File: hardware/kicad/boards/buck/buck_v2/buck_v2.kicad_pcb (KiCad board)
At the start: 2 copper layers, 104 x 104 mm, 23 parts, among them J1 MCP PWM, J2 9V Battery, J3 Conn_01x02_Socket, Q1 IRF530, SW1 Switch, U1 LM7805, U2 4N25, U3 NE555

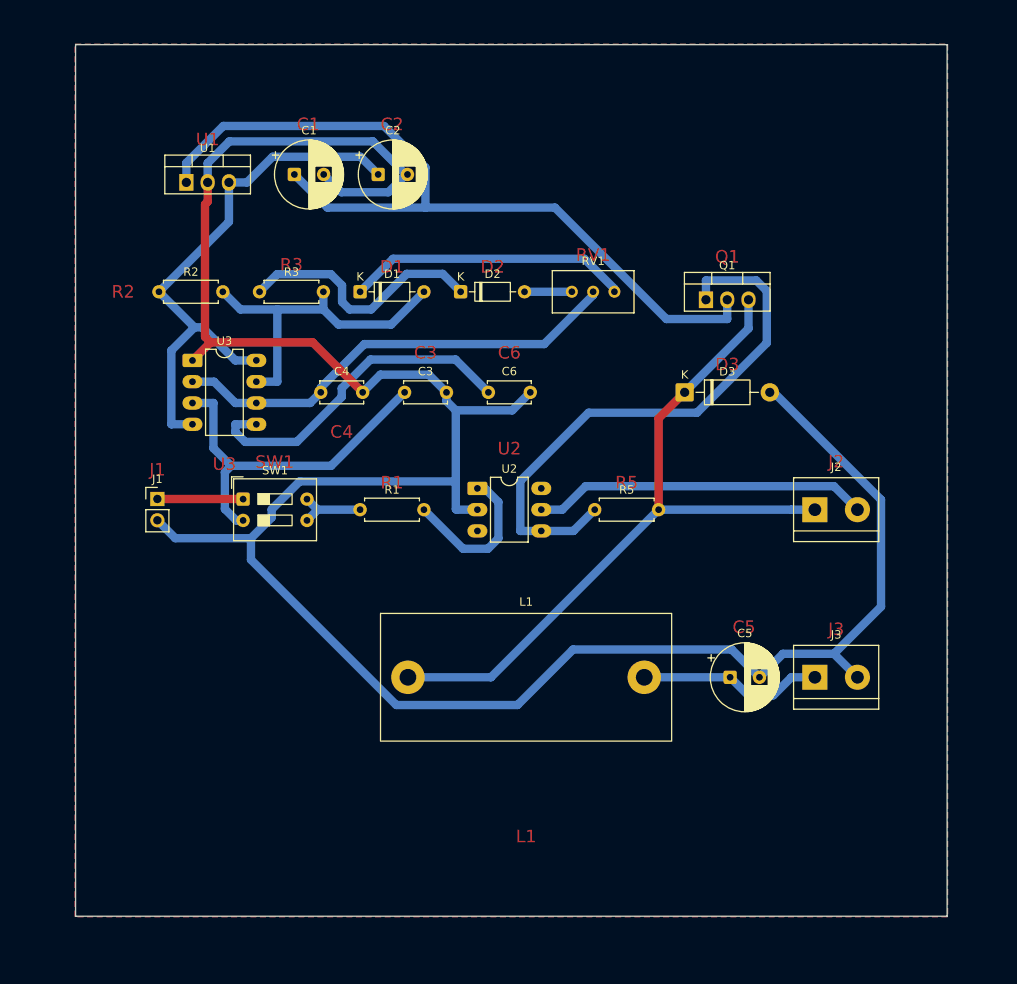
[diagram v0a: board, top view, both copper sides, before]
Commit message: buck_v2: skil batteriet fra Rectifier-nettet igen og genbyg printet
Omtegningen ved batteriet havde kortsluttet batteri+ med Rectifier (V1) -
15V-skinnen ville lade 9V-batteriet baglaens, og gate-forsyningens flyden
paa SW var brudt (se forklaringen i PCB-noterne: batteriet maa kun roere
opto-kollektoren og SW). Broen er fjernet; det nye Rectifier-label ved U1
beholdes som V1-foedning til LM7805. PWR_FLAG flyttet med.

PLACE-layoutet og BOM-raekkerne fulgt op paa re-annoteringen (555=U2,
opto=U3, batteri=J1 osv.). Genroutet: 9 topbaner (31 mm), 0 vias, DRC 0
fejl. Nye DXF/gerbers i production/buck_v2/.
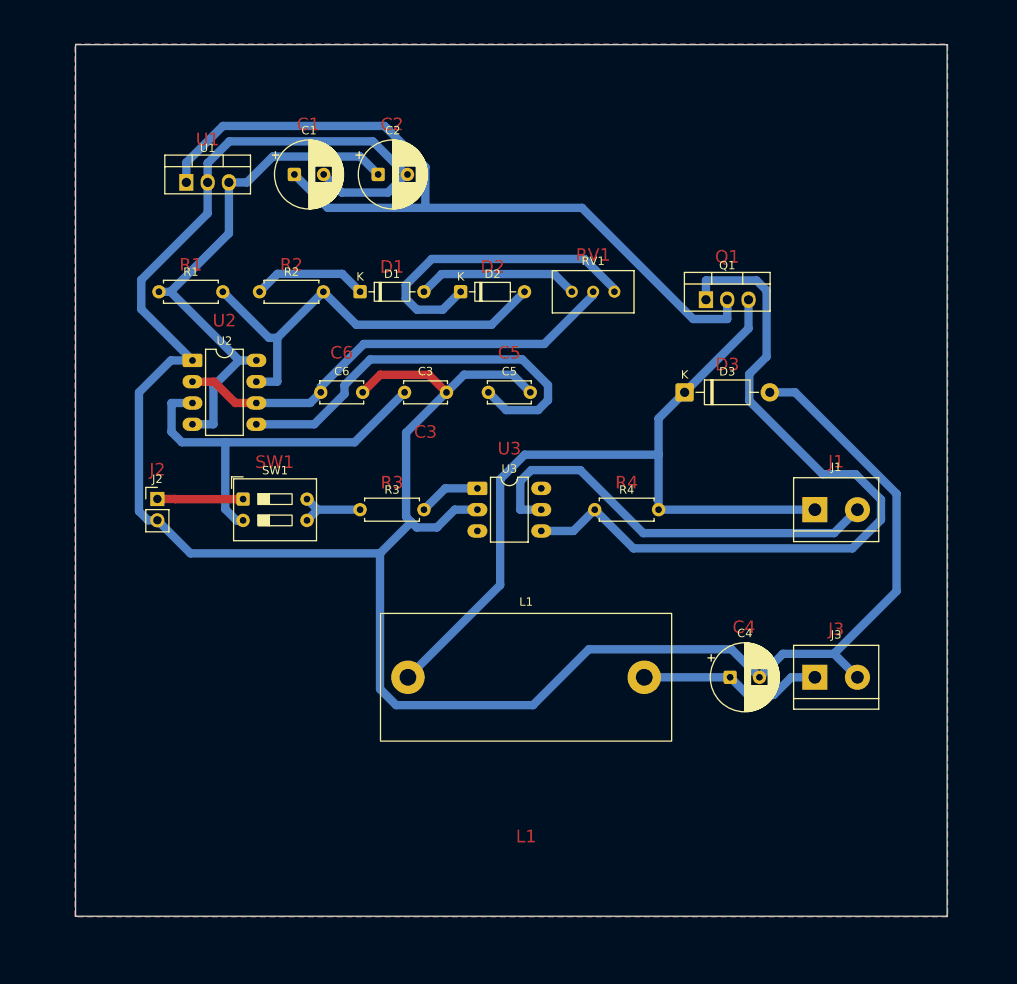
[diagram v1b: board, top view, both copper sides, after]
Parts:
- removed R5: 1k, R_Axial_DIN0207_L6.3mm_D2.5mm_P7.62mm_Horizontal
- added R4: 1k, R_Axial_DIN0207_L6.3mm_D2.5mm_P7.62mm_Horizontal, F.Cu at (82.0, 75.5)
- C4: value 8n2 -> 47u; footprint C_Disc_D5.0mm_W2.5mm_P5.00mm -> CP_Radial_D8.0mm_P3.50mm
- C5: value 47u -> 100n; footprint CP_Radial_D8.0mm_P3.50mm -> C_Disc_D5.0mm_W2.5mm_P5.00mm
- C6: value 100n -> 8n2
- J1: value MCP PWM -> 9V Battery; footprint PinHeader_1x02_P2.54mm_Vertical -> TerminalBlock_bornier-2_P5.08mm
- J2: value 9V Battery -> MCP PWM; footprint TerminalBlock_bornier-2_P5.08mm -> PinHeader_1x02_P2.54mm_Vertical
- R1: value 200R -> 10k
- R3: value 10k -> 200R
- U2: value 4N25 -> NE555; footprint DIP-6_W7.62mm_LongPads -> DIP-8_W7.62mm_LongPads
- U3: value NE555 -> 4N25; footprint DIP-8_W7.62mm_LongPads -> DIP-6_W7.62mm_LongPads
- moved J1 78.5 mm to (108.2, 75.5)
- moved J2 78.5 mm to (29.8, 74.2)
- moved C4 59.5 mm to (98.1, 95.5)
- moved C5 44.6 mm to (69.3, 61.5)
- moved U2 37.3 mm to (34.0, 57.7)
- moved U3 37.3 mm to (68.0, 72.9)
- moved R1 35.4 mm to (29.9, 49.5)
- moved R3 28.6 mm to (54.0, 75.5)
- moved C6 20.0 mm to (49.3, 61.5)
- moved R2 12.0 mm to (42.0, 49.5)
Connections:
- C3 pad 1: Net-(U3-OUT) -> Net-(U2-OUT)
- C4 pad 1: Net-(U3-THRES) -> Net-(J3-Pin_1)
- C5 pad 1: Net-(J3-Pin_1) -> Net-(U2-CONT)
- C6 pad 1: Net-(U3-CONT) -> Net-(U2-THRES)
- J1 pad 1: Net-(J1-Pin_1) -> /SW
- J1 pad 2: /GND -> /+9V_SW
- J2 pad 1: /SW -> Net-(J2-Pin_1)
- J2 pad 2: /+9V_SW -> /GND
- R1 pad 1: Net-(R1-Pad1) -> Net-(U1-VO)
- R1 pad 2: Net-(R1-Pad2) -> Net-(D2-A)
- R2 pad 1: Net-(U1-VO) -> Net-(D1-K)
- R2 pad 2: Net-(D1-A) -> Net-(D2-A)
- R3 pad 1: Net-(D2-K) -> Net-(R3-Pad1)
- R3 pad 2: Net-(D1-A) -> Net-(R3-Pad2)
- RV1 pad 1: Net-(D1-K) -> Net-(D2-K)
- RV1 pad 2: Net-(U3-THRES) -> Net-(U2-THRES)
- RV1 pad 3: Net-(D2-A) -> Net-(D1-A)
- SW1 pad 1: Net-(J1-Pin_1) -> Net-(J2-Pin_1)
- SW1 pad 2: Net-(U3-OUT) -> Net-(U2-OUT)
- SW1 pad 3: Net-(R1-Pad1) -> Net-(R3-Pad1)
- SW1 pad 4: Net-(R1-Pad1) -> Net-(R3-Pad1)
- U2 pad 1: Net-(R1-Pad2) -> /GND
- U2 pad 2: /GND -> Net-(U2-THRES)
- U2 pad 3: (no net) -> Net-(U2-OUT)
- U2 pad 4: Net-(Q1-PadG) -> Net-(U1-VO)
- U2 pad 5: /+9V_SW -> Net-(U2-CONT)
- U2 pad 6: (no net) -> Net-(U2-THRES)
- U3 pad 1: /GND -> Net-(R3-Pad2)
- U3 pad 2: Net-(U3-THRES) -> /GND
- U3 pad 3: Net-(U3-OUT) -> (no net)
- U3 pad 4: Net-(U1-VO) -> Net-(Q1-PadG)
- U3 pad 5: Net-(U3-CONT) -> /+9V_SW
- U3 pad 6: Net-(U3-THRES) -> (no net)
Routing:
- net Net-(U2-THRES): track 0.00 -> 55.0 mm
- net Net-(U3-THRES): track 54.9 -> 0.00 mm
- net Net-(U2-CONT): track 0.00 -> 50.2 mm
- net Net-(U2-OUT): track 0.00 -> 47.4 mm
- net Net-(D2-A): track 5.65 -> 51.5 mm
- net Net-(U3-OUT): track 43.4 -> 0.00 mm
- net Net-(U3-CONT): track 40.4 -> 0.00 mm
- net Net-(Q1-PadG): track 68.4 -> 92.0 mm
- net Net-(D1-A): track 40.5 -> 19.4 mm
- net Net-(D1-K): track 33.8 -> 13.8 mm
- net Net-(R1-Pad2): track 18.8 -> 0.00 mm
- net /+9V_SW: track 40.1 -> 51.0 mm
- net Net-(J1-Pin_1): track 10.2 -> 0.00 mm
- net Net-(J2-Pin_1): track 0.00 -> 10.2 mm
- net /SW: track 86.3 -> 96.5 mm
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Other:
- board text added: "R4"
- board text removed: "R5"

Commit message: Boost v2 med IR2110 gate-driver + boost test-resultater
- boost_v2: integreret IR2110 gate-drive (opto -> IR2110 -> low-side MOSFET),
  generator (build_boost_v2.py), schematic, board og laser/gerber-filer
- buck_v2: patchet til IR2110 high-side drive (patch_buck_v2_ir2110.py)
- boost: opdateret board, gamle produktions-DXF erstattet af boost_v2
- AD3 boost-bringup script (tools/ad3/boost_test.py)
- BOM opdateret med IR2110/CNY17; CNY17- og IRF530-datablade
- rapport: boost maaleresultater (10 kHz, 40%) med figur
- HANDOFF-dokument for buck/boost IR2110-redesign; PCB_RESULTS opdateret
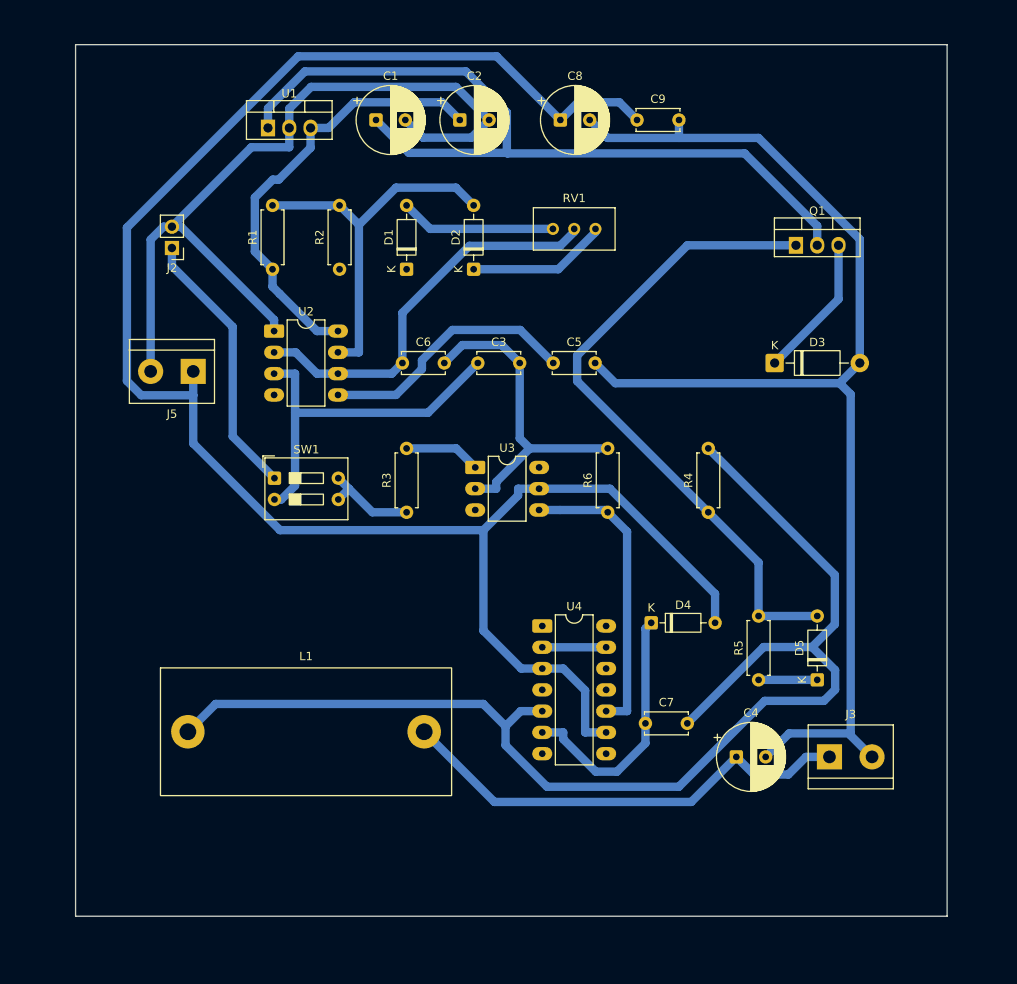
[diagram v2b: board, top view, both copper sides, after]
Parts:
- removed J1: 9V Battery, TerminalBlock_bornier-2_P5.08mm
- added C7: 1u, C_Disc_D5.0mm_W2.5mm_P5.00mm, F.Cu at (88.0, 101.0)
- added C8: 22u, CP_Radial_D8.0mm_P3.50mm, F.Cu at (77.8, 29.0)
- added C9: 100n, C_Disc_D5.0mm_W2.5mm_P5.00mm, F.Cu at (87.0, 29.0)
- added D4: 1N4148, D_DO-35_SOD27_P7.62mm_Horizontal, F.Cu at (88.7, 89.0)
- added D5: 1N4148, D_DO-35_SOD27_P7.62mm_Horizontal, F.Cu at (108.5, 95.8)
- added J5: drive +15V, TerminalBlock_bornier-2_P5.08mm, F.Cu at (34.0, 59.0)
- added R5: 10, R_Axial_DIN0207_L6.3mm_D2.5mm_P7.62mm_Horizontal, F.Cu at (101.5, 95.8)
- added R6: 1k, R_Axial_DIN0207_L6.3mm_D2.5mm_P7.62mm_Horizontal, F.Cu at (83.5, 75.8)
- added U4: IR2110, DIP-14_W7.62mm_LongPads, F.Cu at (75.7, 89.4)
- moved J2 30.0 mm to (31.5, 44.3), turned to 180 degrees
- moved L1 27.1 mm to (33.4, 102.0)
- moved R1 13.8 mm to (43.5, 46.8), turned to 90 degrees
- moved R4 13.6 mm to (95.5, 75.8), turned to 90 degrees
- moved Q1 12.6 mm to (106.0, 43.9)
- moved U1 11.7 mm to (43.0, 29.9)
- moved C2 11.7 mm to (65.8, 29.0)
- moved C1 11.7 mm to (55.8, 29.0)
- moved D3 11.3 mm to (103.4, 58.0)
- moved C6 10.3 mm to (59.0, 58.0)
- moved U2 10.3 mm to (43.7, 54.2)
- moved R2 9.92 mm to (51.5, 46.8), turned to 90 degrees
- moved J3 9.66 mm to (110.0, 105.0)
- moved C4 9.53 mm to (98.8, 105.0)
- moved C3 9.41 mm to (68.0, 58.0)
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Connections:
- Q1 pad 1: Net-(Q1-PadG) -> /GATE
- R4 pad 1: Net-(Q1-PadG) -> /GATE
- U3 pad 4: Net-(Q1-PadG) -> /HIN
- U3 pad 5: /+9V_SW -> /+15V
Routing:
- net /+15V: track 0.00 -> 222.1 mm
- net Net-(Q1-PadG): track 92.0 -> 0.00 mm
- net /GATE: track 0.00 -> 78.6 mm
- net /SW: track 96.5 -> 167.1 mm
- net /+9V_SW: track 51.0 -> 0.00 mm
- net /HIN: track 0.00 -> 35.5 mm
- net Net-(J3-Pin_1): track 22.1 -> 55.8 mm
- net /VB: track 0.00 -> 30.8 mm
- net Net-(J2-Pin_1): track 10.2 -> 32.5 mm
- net Net-(D2-K): track 37.6 -> 16.8 mm
- net Net-(U2-CONT): track 50.2 -> 31.1 mm
- net Net-(D1-K): track 13.8 -> 0.00 mm
- net Net-(U1-VO): track 62.3 -> 52.9 mm
- net /GND: track 300.1 -> 291.3 mm
- net Net-(U2-THRES): track 55.0 -> 47.7 mm
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- removed copper zone on B.Cu, net (none)
- removed copper zone on F.Cu, net (none)
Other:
- board text removed: "C1"
- board text removed: "C2"
- board text removed: "C3"
- board text removed: "C4"
- board text removed: "C5"
- board text removed: "C6"
- board text removed: "D1"
- board text removed: "D2"
- board text removed: "D3"
- board text removed: "J1"
- board text removed: "J2"
- board text removed: "J3"
- board text removed: "L1"
- board text removed: "Q1"
- board text removed: "R1"
- board text removed: "R2"
- board text removed: "R3"
- board text removed: "R4"
- board text removed: "RV1"
- board text removed: "SW1"
- board text removed: "U1"
- board text removed: "U2"
- board text removed: "U3"

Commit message: Buck_v2 routet + MPPT-buck board + audit/handoff
- buck_v2: enkeltsidet route faerdig (0 uroutede, 0 vias, 8 traadbroer);
  C6 8n2 box-footprint; faerdige laser-DXF; placerings-SVG matcher boardet
- mppt_buck: ny switching-buck til MPPT (PV ~17.6V -> 5V lager, IR2110
  high-side, Arduino P&O) - board, generator (build_mppt_buck.py), produktion
- BOM/footprint_map + PCB_RESULTS opdateret
- AUDIT (buck/boost IR2110) + HANDOFF (mppt buck) dokumenter
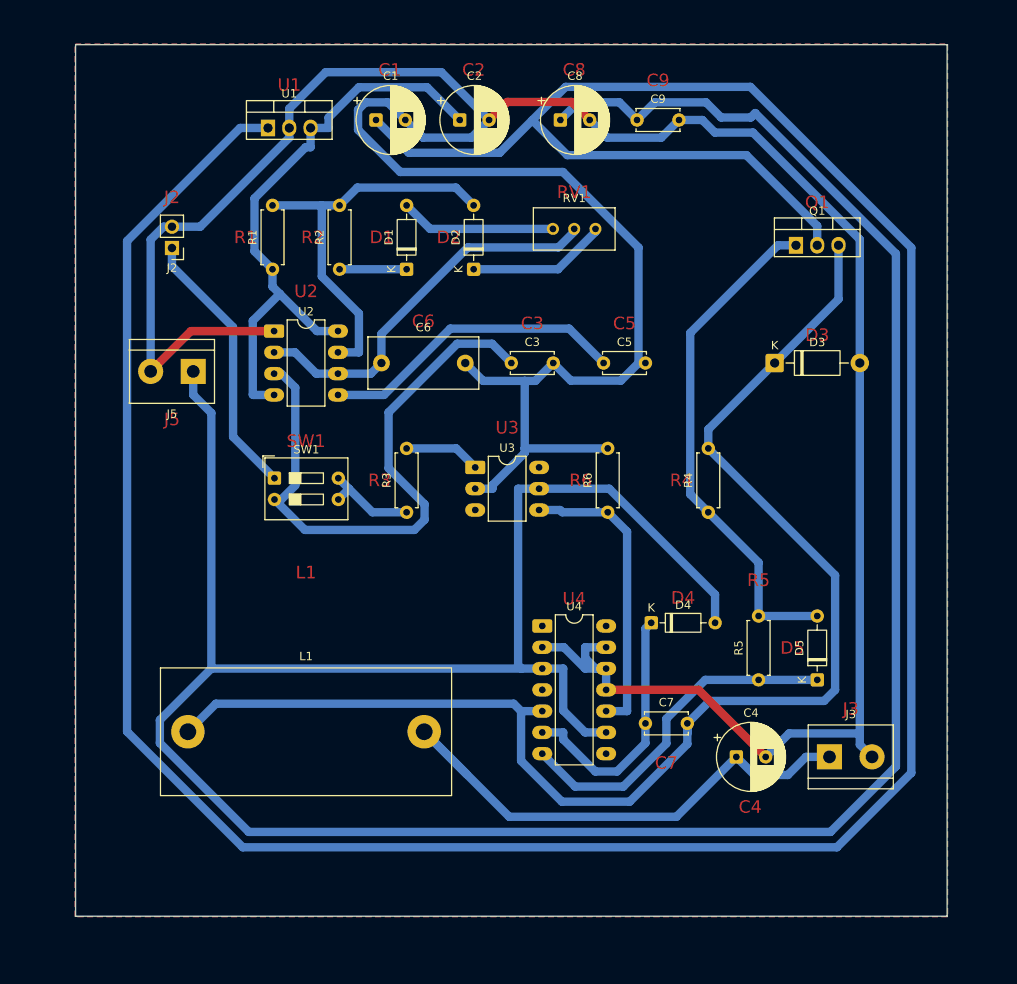
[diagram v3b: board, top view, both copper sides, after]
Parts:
- C6: footprint C_Disc_D5.0mm_W2.5mm_P5.00mm -> C_Rect_L13.0mm_W6.0mm_P10.00mm_FKS3_FKP3_MKS4
- moved C5 6.00 mm to (83.0, 58.0)
- moved C3 4.00 mm to (72.0, 58.0)
- moved C6 2.50 mm to (56.5, 58.0)
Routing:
- net Rectifier: track 99.7 -> 364.8 mm
- net /+15V: track 222.1 -> 361.9 mm
- net /GND: track 291.3 -> 378.5 mm
- net /HO: track 7.00 -> 41.4 mm
- net Net-(U2-OUT): track 43.3 -> 71.6 mm
- net Net-(U1-VO): track 52.9 -> 71.0 mm
- net /GATE: track 78.6 -> 61.1 mm
- net Net-(J3-Pin_1): track 55.8 -> 64.5 mm
- net Net-(D1-K): track 0.00 -> 8.00 mm
- net Net-(U2-CONT): track 31.1 -> 36.7 mm
- net /SW: track 167.1 -> 163.4 mm
- net Net-(D2-A): track 45.4 -> 47.6 mm
- net Net-(U2-THRES): track 47.7 -> 46.3 mm
- added copper zone on B.Cu, net (none)
- added copper zone on F.Cu, net (none)
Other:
- board text added: "C1"
- board text added: "C2"
- board text added: "C3"
- board text added: "C4"
- board text added: "C5"
- board text added: "C6"
- board text added: "C7"
- board text added: "C8"
- board text added: "C9"
- board text added: "D1"
- board text added: "D2"
- board text added: "D3"
- board text added: "D4"
- board text added: "D5"
- board text added: "J2"
- board text added: "J3"
- board text added: "J5"
- board text added: "L1"
- board text added: "Q1"
- board text added: "R1"
- board text added: "R2"
- board text added: "R3"
- board text added: "R4"
- board text added: "R5"
- board text added: "R6"
- board text added: "RV1"
- board text added: "SW1"
- board text added: "U1"
- board text added: "U2"
- board text added: "U3"
- board text added: "U4"
